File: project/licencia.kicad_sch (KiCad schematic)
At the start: 0 parts

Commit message: cambio a nombre final, agregado de licencia en esquematico y etiqueta
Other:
- company: (none) -> Maximiliano Simonazzi, Valentin Gomez Espeche
- title: (none) -> Azukar FPGA
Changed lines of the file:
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@@
 	(generator_version "9.0")
 	(paper "A4")
+	(title_block
+		(title "Azukar FPGA")
+		(date "2026-02-04")
+		(rev "1.4")
+		(company "Maximiliano Simonazzi, Valentin Gomez Espeche")
+		(comment 1 "attribution to the original AZUKAR project is preserved.")
+		(comment 2 "This design may be copied, modified, manufactured, and distributed provided that")
+		(comment 3 "Year: 2026")
+		(comment 4 "License: CERN Open Hardware Licence v2 – Permissive (CERN-OHL-P-2.0)")
+	)
 	(text "# English\n\nThis design is released under the CERN Open Hardware Licence v2 - Permissive (CERN-OHL-P-2.0).\n\nYou are free to copy, modify, manufacture, and distribute this design, provided that attribution\nto the original AZUKAR project is preserved.\n\nThis is an independent hardware design based on publicly available documentation of the Lattice\niCE40HX FPGA family. It is not affiliated with or endorsed by Lattice Semiconductor."
 		(exclude_from_sim no)

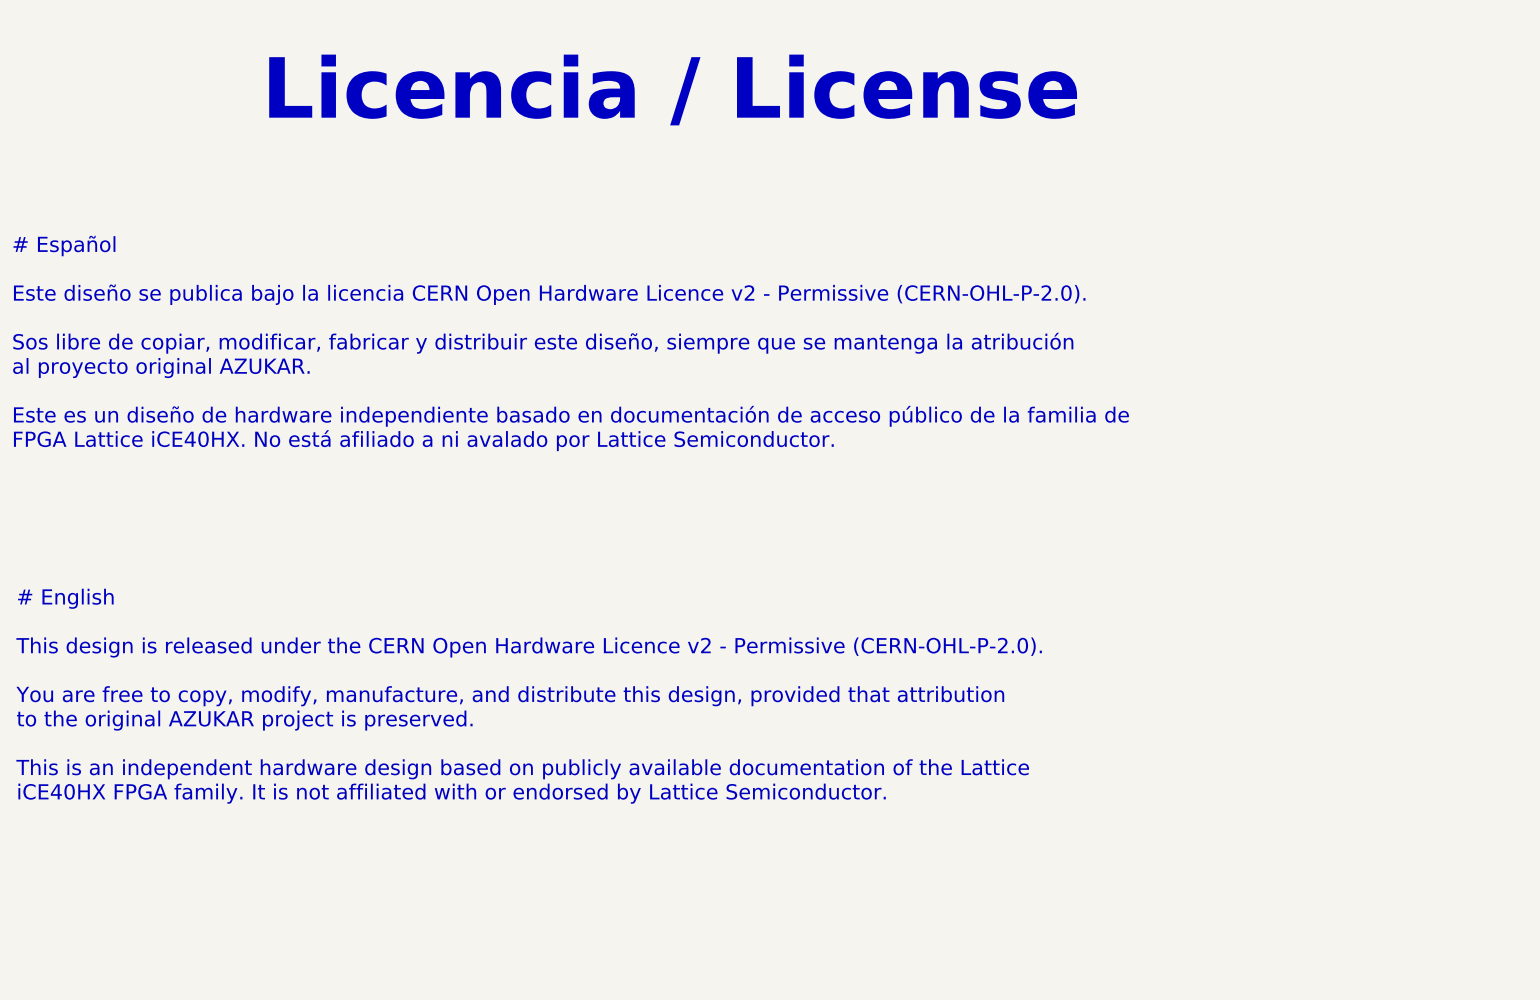
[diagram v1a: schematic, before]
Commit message: Eliminar mensaje de error - Issue #8. Mejora en algunas trazas del PCB, eliminacion de algunas vias ordenando mejor los componentes.
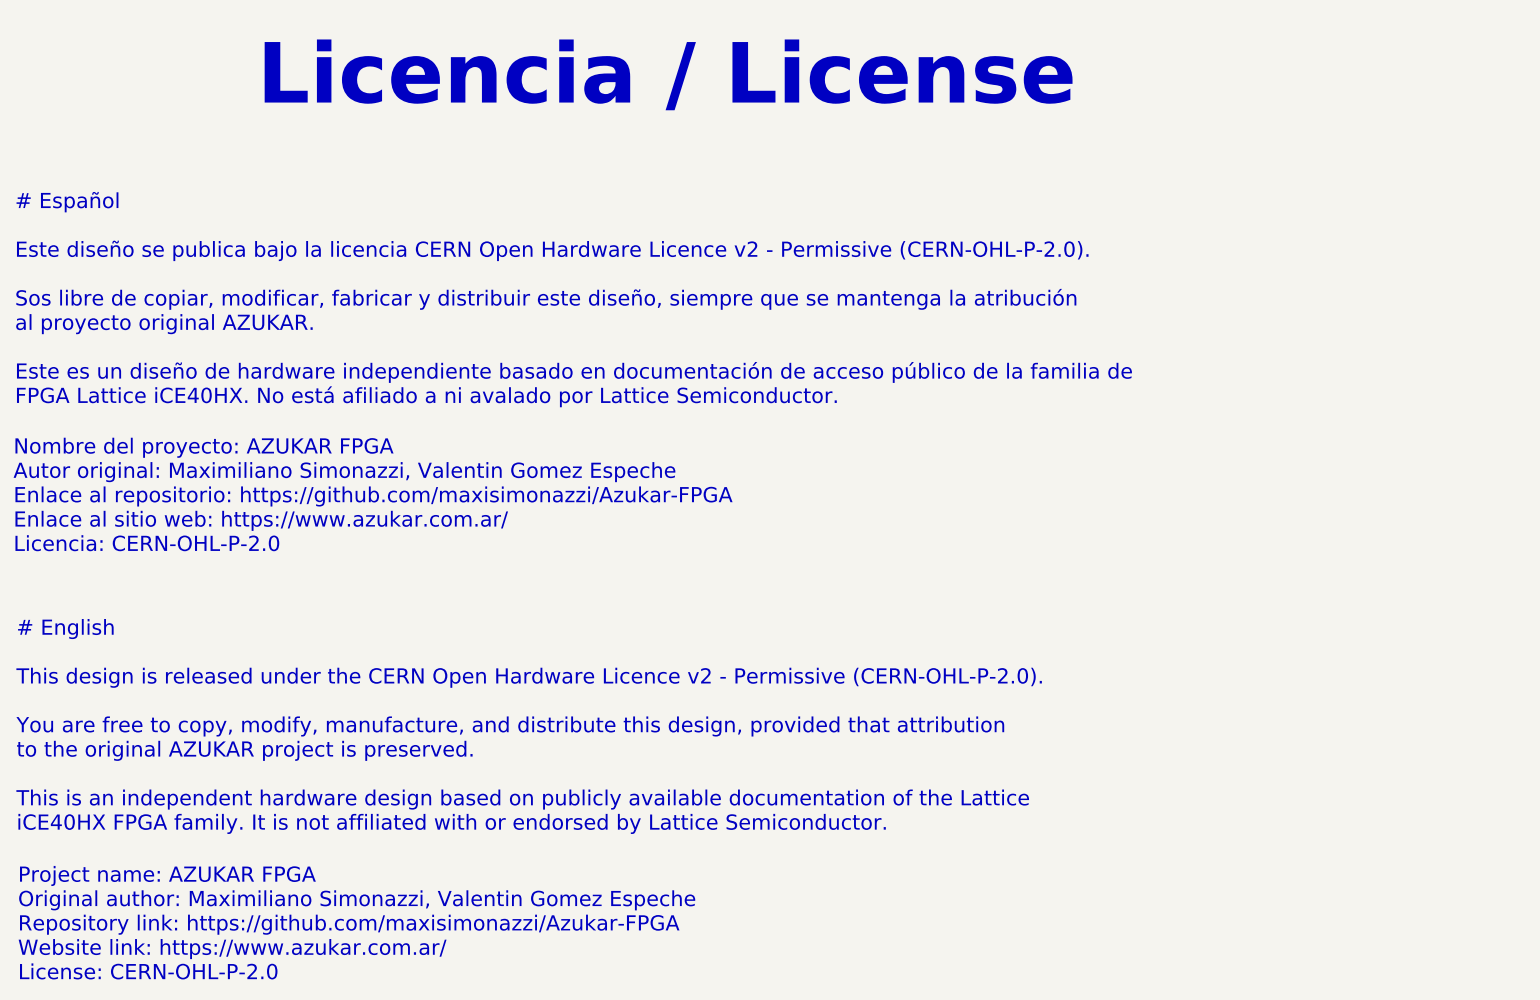
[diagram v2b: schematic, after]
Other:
- note added: "Nombre del proyecto: AZUKAR FPGA Autor original: Maximiliano Simonazzi, Valentin Gomez Espeche Enlace al repositorio: https://github.com/maxisimonazzi/Azukar-FPGA Enlace al sitio web: https://www.azukar.com.ar/ Licencia: CERN-OHL-P-2.0"
- note added: "Project name: AZUKAR FPGA Original author: Maximiliano Simonazzi, Valentin Gomez Espeche Repository link: https://github.com/maxisimonazzi/Azukar-FPGA Website link: https://www.azukar.com.ar/ License: CERN-OHL-P-2.0"
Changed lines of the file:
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@@
 	(text "# English\n\nThis design is released under the CERN Open Hardware Licence v2 - Permissive (CERN-OHL-P-2.0).\n\nYou are free to copy, modify, manufacture, and distribute this design, provided that attribution\nto the original AZUKAR project is preserved.\n\nThis is an independent hardware design based on publicly available documentation of the Lattice\niCE40HX FPGA family. It is not affiliated with or endorsed by Lattice Semiconductor."
 		(exclude_from_sim no)
-		(at 38.862 132.334 0)
+		(at 38.862 137.414 0)
 		(effects
 			(font
@@
 	(text "# Español\n\nEste diseño se publica bajo la licencia CERN Open Hardware Licence v2 - Permissive (CERN-OHL-P-2.0).\n\nSos libre de copiar, modificar, fabricar y distribuir este diseño, siempre que se mantenga la atribución\nal proyecto original AZUKAR.\n\nEste es un diseño de hardware independiente basado en documentación de acceso público de la familia de\nFPGA Lattice iCE40HX. No está afiliado a ni avalado por Lattice Semiconductor."
 		(exclude_from_sim no)
-		(at 38.1 73.152 0)
+		(at 38.608 65.786 0)
 		(effects
 			(font
@@
 		)
 	)
+	(text "Project name: AZUKAR FPGA\nOriginal author: Maximiliano Simonazzi, Valentin Gomez Espeche\nRepository link: https://github.com/maxisimonazzi/Azukar-FPGA\nWebsite link: https://www.azukar.com.ar/\nLicense: CERN-OHL-P-2.0"
+		(exclude_from_sim no)
+		(at 39.116 170.688 0)
+		(effects
+			(font
+				(size 2.54 2.54)
+				(thickness 0.3175)
+			)
+			(justify left)
+		)
+	)
 	(text "Licencia / License"
 		(exclude_from_sim no)
-		(at 80.01 30.734 0)
+		(at 79.248 28.194 0)
 		(effects
 			(font
@@
 				(thickness 2.032)
 				(bold yes)
+				(color 132 0 0 1)
 			)
 			(justify left)
+		)
+	)
+	(text "Nombre del proyecto: AZUKAR FPGA\nAutor original: Maximiliano Simonazzi, Valentin Gomez Espeche\nEnlace al repositorio: https://github.com/maxisimonazzi/Azukar-FPGA\nEnlace al sitio web: https://www.azukar.com.ar/\nLicencia: CERN-OHL-P-2.0"
+		(exclude_from_sim no)
+		(at 38.354 98.806 0)
+		(effects
+			(font
+				(size 2.54 2.54)
+			)
+			(justify left)

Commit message: pequeño rework a la pcb
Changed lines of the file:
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@@
 			(font
 				(size 2.54 2.54)
-				(thickness 0.3175)
+				(thickness 0.508)
+				(bold yes)
 			)
 			(justify left)
@@
 			(font
 				(size 2.54 2.54)
+				(thickness 0.508)
+				(bold yes)
 			)
 			(justify left)
